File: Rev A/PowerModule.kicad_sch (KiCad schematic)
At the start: 20 parts, among them K1 Relay_SPDT, Q1 IRLZ44N, U1 LM741

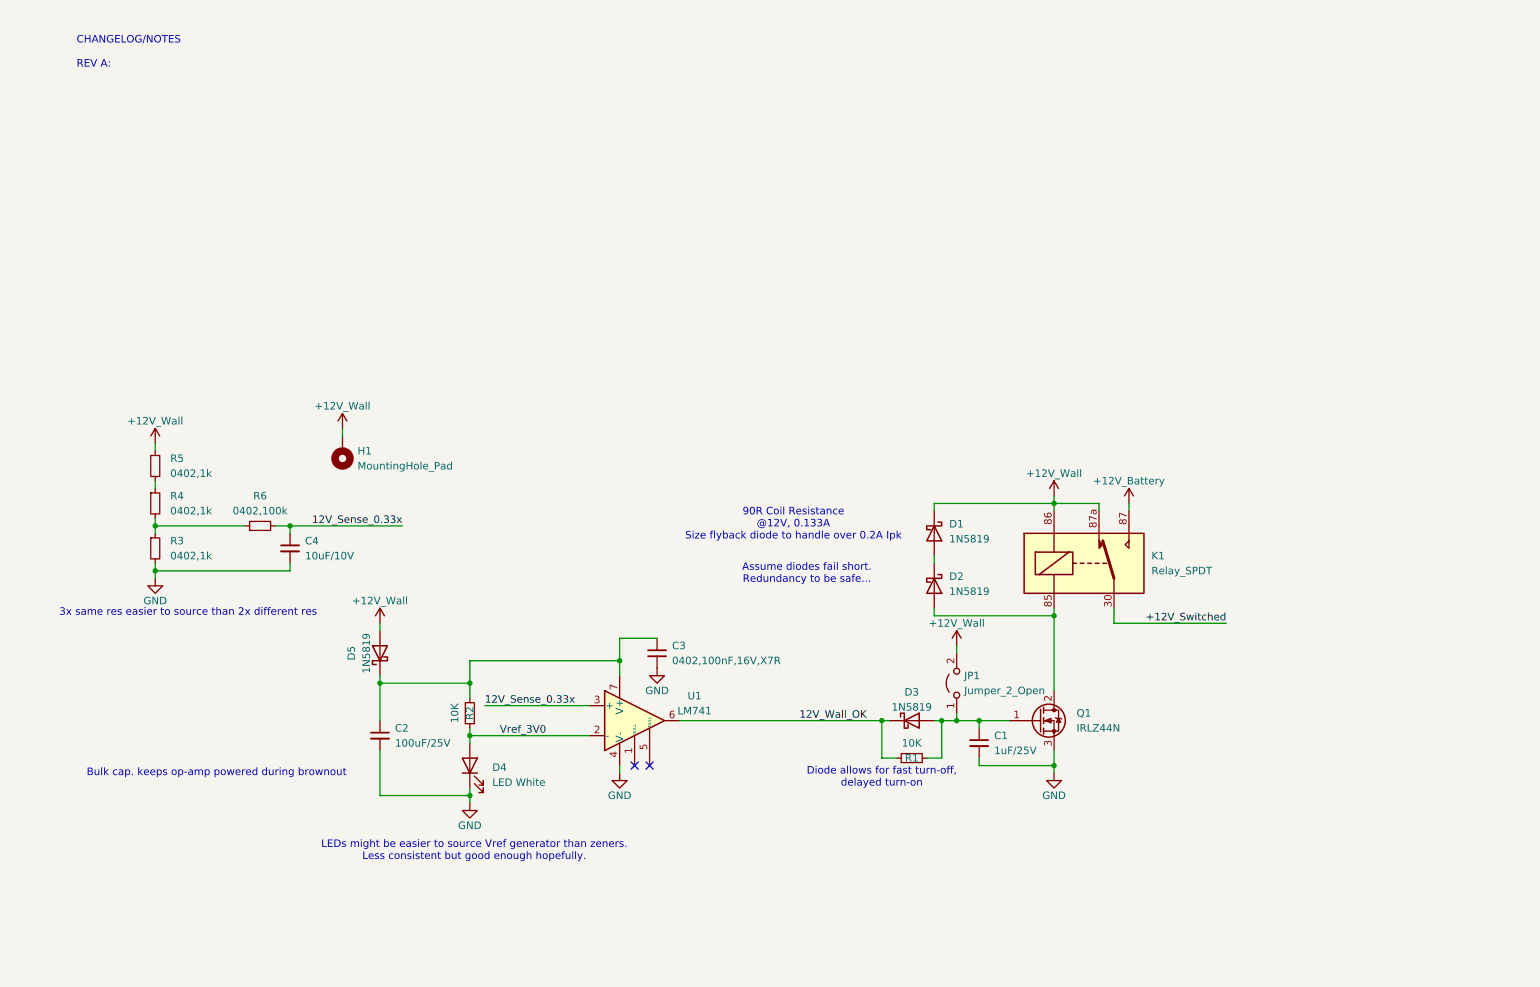
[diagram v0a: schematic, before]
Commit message: added simulation stuff
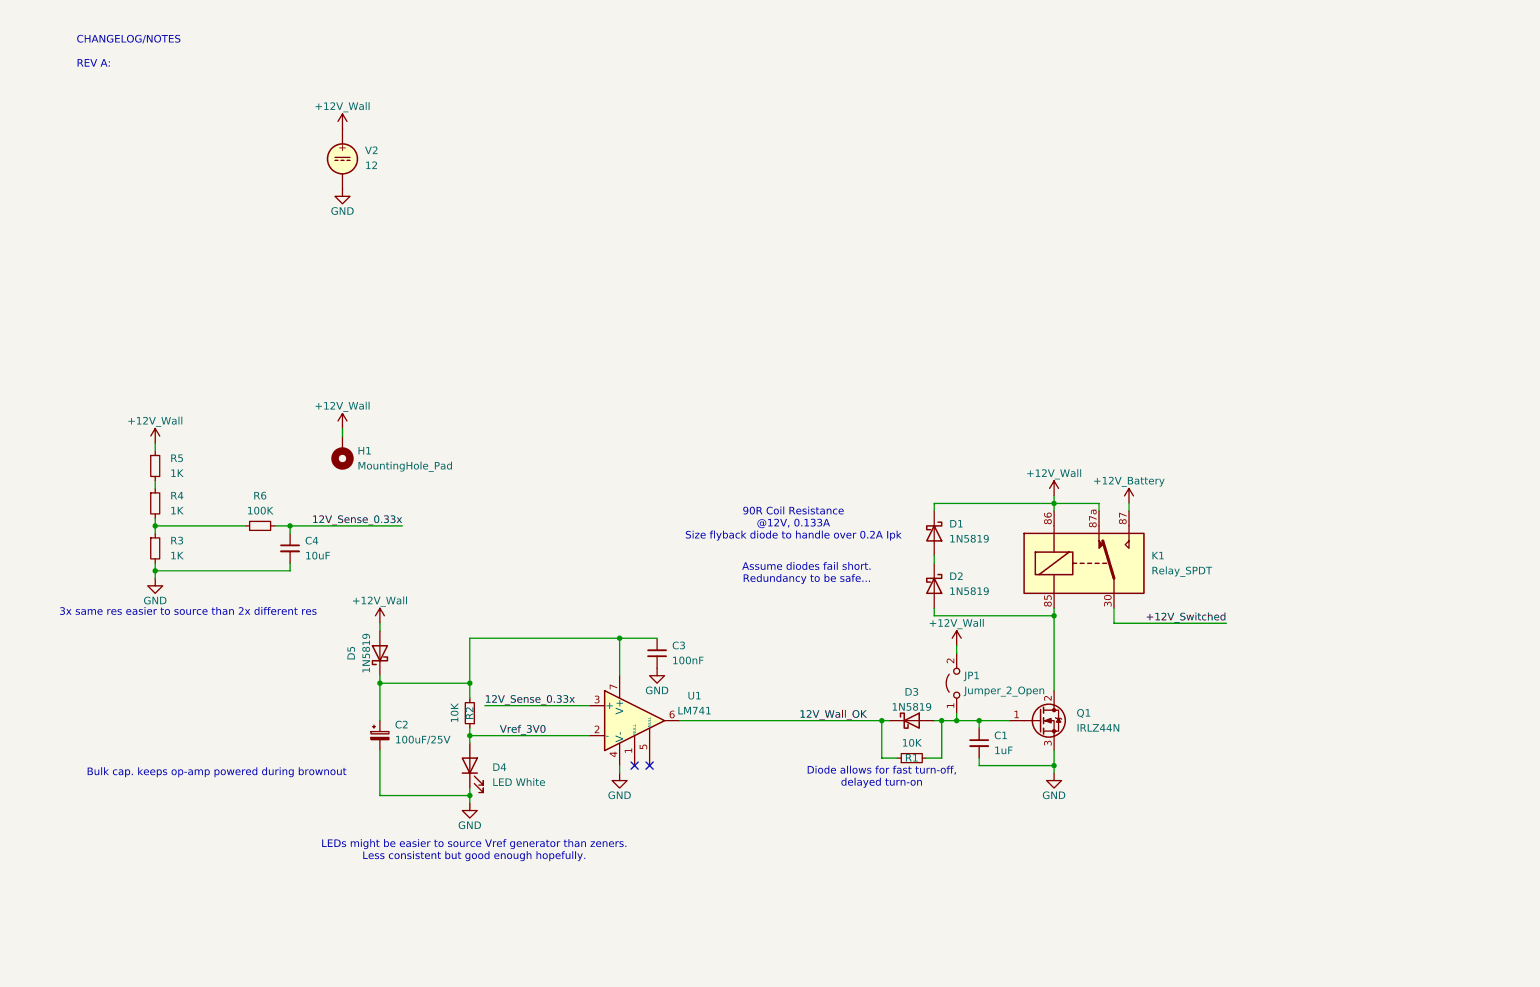
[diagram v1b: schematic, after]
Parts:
- removed C2: 100uF/25V, symbol Device:C_Small
- added C2: 100uF/25V, symbol Device:C_Polarized_Small
- added V2: 12, symbol Simulation_SPICE:VDC
- C1: value 1uF/25V -> 1uF
- C3: value 0402,100nF,16V,X7R -> 100nF
- C4: value 10uF/10V -> 10uF
- R3, R4, R5: value 0402,1k -> 1K
- R6: value 0402,100k -> 100K
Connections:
- net +12V_Wall: now also V2.1
- net GND: now also C2.2, V2.2
- net at C3.1, D5.1 (K), R2.2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: now also C2.1

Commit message: Added all schematic parts, started layout
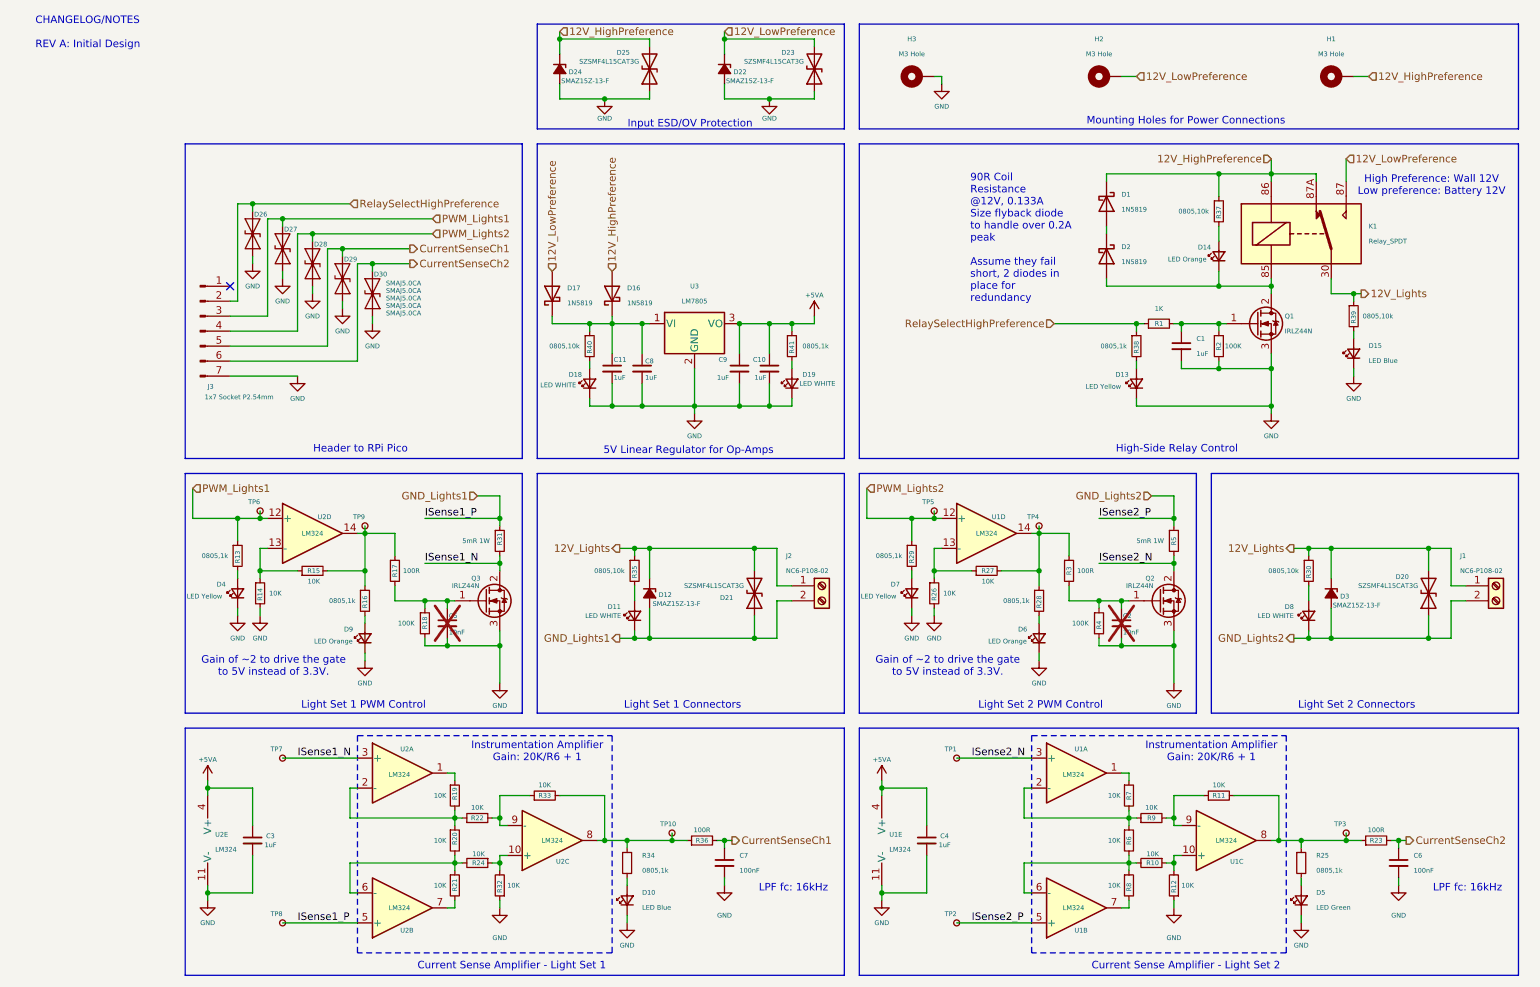
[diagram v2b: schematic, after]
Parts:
- removed C2: 100uF/25V, symbol Device:C_Polarized_Small
- removed C3: 100nF, C_0402_1005Metric, symbol jlcpcb-basic-capacitor:0402,100nF,16V,X7R
- removed D3, D5: 1N5819, Diode_THT:D_DO-41_SOD81_P10.16mm_Horizontal, symbol Diode:1N5819
- removed D4: LED White, symbol Device:LED
- removed JP1: Jumper_2_Open, symbol Jumper:Jumper_2_Open
- removed R1, R2: 10K, symbol Device:R_Small
- removed R4, R5: 1K, R_0402_1005Metric, symbol jlcpcb-basic-resistor:0402,1k
- removed R6: 100K, R_0402_1005Metric, symbol jlcpcb-basic-resistor:0402,100k
- removed U1: LM741, symbol Amplifier_Operational:LM741
- removed V2: 12, symbol Simulation_SPICE:VDC
- added C10, C11, C3, C8, C9: 1uF, Capacitor_SMD:C_0805_2012Metric, symbol Device:C_Small
- added C2, C5: 10nF, Capacitor_SMD:C_0805_2012Metric, symbol Device:C_Small
- added C6, C7: 100nF, Capacitor_SMD:C_0805_2012Metric, symbol Device:C_Small
- added D10, D15: LED Blue, LED_SMD:LED_0805_2012Metric, symbol Device:LED_Small
- added D11, D18, D19, D8: LED WHITE, LED_SMD:LED_0805_2012Metric, symbol Device:LED_Small
- added D12, D22, D24, D3: SMAZ15Z-13-F, Diode_SMD:D_SMA, symbol Device:D_Zener_Small_Filled
- added D13, D4, D7: LED Yellow, LED_SMD:LED_0805_2012Metric, symbol Device:LED_Small
- added D14, D6, D9: LED Orange, LED_SMD:LED_0805_2012Metric, symbol Device:LED_Small
- added D16, D17: 1N5819, Diode_THT:D_DO-41_SOD81_P10.16mm_Horizontal, symbol Diode:1N5819
- added D20, D21, D23, D25: SZSMF4L15CAT3G, Diode_SMD:D_SOD-123F, symbol Device:D_TVS
- added D26, D27, D28, D29, D30: SMAJ5.0CA, Diode_SMD:D_SMA, symbol Diode:SMAJ5.0CA
- added D5: LED Green, LED_SMD:LED_0805_2012Metric, symbol Device:LED_Small
- added H2, H3: M3 Hole, MountingHole:MountingHole_3.2mm_M3_Pad_TopBottom, symbol Mechanical:MountingHole_Pad
- added J1, J2: NC6-P108-02, TerminalBlock_MetzConnect:TerminalBlock_MetzConnect_Type703_RT10N02HGLU_1x02_P9.52mm_Horizontal, symbol Connector:Screw_Terminal_01x02
- added J3: 1x7 Socket P2.54mm, Connector_PinSocket_2.54mm:PinSocket_1x07_P2.54mm_Vertical, symbol Connector:Conn_01x07_Pin
- added Q2, Q3: IRLZ44N, Package_TO_SOT_THT:TO-220-3_Horizontal_TabDown, symbol Transistor_FET:IRLZ44N
- added R1: 1K, Resistor_SMD:R_0805_2012Metric, symbol jlcpcb-basic-resistor:0402,1k
- added R10, R11, R12, R14, R15, R19, R20, R21, R22, R24, R26, R27, R32, R33, R6, R7, R8, R9: 10K, Resistor_SMD:R_0805_2012Metric, symbol jlcpcb-basic-resistor:0402,10k
- added R13, R16, R25, R28, R29, R34, R38, R41: 0805,1k, Resistor_SMD:R_0805_2012Metric, symbol jlcpcb-basic-resistor:0805,1k
- added R17: 100R, Resistor_SMD:R_0805_2012Metric, symbol jlcpcb-basic-resistor:0402,1k
- added R18, R2, R4: 100K, Resistor_SMD:R_0805_2012Metric, symbol jlcpcb-basic-resistor:0402,100k
- added R23, R36: 100R, Resistor_SMD:R_0805_2012Metric, symbol jlcpcb-basic-resistor:0402,10k
- added R30, R35, R37, R39, R40: 0805,10k, Resistor_SMD:R_0805_2012Metric, symbol jlcpcb-basic-resistor:0805,10k
- added R31, R5: 5mR 1W, Resistor_SMD:R_2512_6332Metric, symbol Device:R_Small
- added TP1, TP10, TP2, TP3, TP4, TP5, TP6, TP7, TP8, TP9: TestPoint_Small, TestPoint:TestPoint_Pad_D2.0mm, symbol Connector:TestPoint_Small
- added U1, U2: LM324, Package_DIP:DIP-14_W7.62mm_Socket, symbol Amplifier_Operational:LM324
- added U3: LM7805, Package_TO_SOT_THT:TO-220-3_Horizontal_TabDown, symbol Regulator_Linear:LM7805_TO220
- C1: footprint (none) -> Capacitor_SMD:C_0805_2012Metric
- C4: value 10uF -> 1uF; footprint (none) -> Capacitor_SMD:C_0805_2012Metric
- H1: value MountingHole_Pad -> M3 Hole; footprint (none) -> MountingHole:MountingHole_3.2mm_M3_Pad_TopBottom; now left out of the parts list
- Q1: footprint Package_TO_SOT_THT:TO-220-3_Vertical -> Package_TO_SOT_THT:TO-220-3_Horizontal_TabDown
- R3: value 1K -> 100R; footprint R_0402_1005Metric -> Resistor_SMD:R_0805_2012Metric
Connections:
- net GND: now also C10.2, C11.2, C2.2, C3.2, C5.2, C6.2, C7.2, C8.2, C9.2, D10.1 (K), D13.1 (K), D15.1 (K), D18.1 (K), D19.1 (K), D22.2 (A), D23.1 (A1), D24.2 (A), D25.1 (A1), D26.1 (A1), D27.1 (A1), D28.1 (A1), D29.1 (A1), D30.1 (A1), D4.1 (K), D5.1 (K), D6.1 (K), D7.1 (K), D9.1 (K), H3.1, J3.7 (Pin_7), Q2.3 (S), Q3.3 (S), R12.1, R14.2, R18.2, R2.2, R26.2, R32.1, R4.2, U1.11 (V-), U2.11 (V-), U3.2 (GND); no longer R3.2
- net at C1.1, Q1.1 (G): now also R1.2, R2.1
- net at D2.2 (A), K1.85, Q1.2 (D): now also D14.1 (K)
- net at R3.1: now also R27.2, R28.1, TP4.1, U1.14
- net +12V_Battery renamed 12V_LowPreference
- net 12V_LowPreference: now also D17.2 (A), D22.1 (K), D23.2 (A2), H2.1
- net +12V_Switched renamed 12V_Lights
- net 12V_Lights: now also D12.1 (K), D20.2 (A2), D21.2 (A2), D3.1 (K), J1.1 (Pin_1), J2.1 (Pin_1), R30.1, R35.1, R39.1
- net +12V_Wall renamed 12V_HighPreference
- net 12V_HighPreference: now also K1.87A, D16.2 (A), D24.1 (K), D25.2 (A2), R37.1; no longer K1.87a
- net 12V_Sense_0.33x renamed +5VA
- net +5VA: now also C10.1, C3.1, C9.1, R41.1, U1.4 (V+), U2.4 (V+), U3.3 (VO)
- new net: D7.2 (A), R29.2
- new net: R19.1, U2.1
- new net: R19.2, R20.1, R22.1, U2.2 (-)
- new net: R33.2, R34.1, R36.1, TP10.1, U2.8
- new net: R15.2, R16.1, R17.1, TP9.1, U2.14
- new net: C5.1, Q3.1 (G), R17.2, R18.1
- new net: D15.2 (A), R39.2
- new net: R22.2, R33.1, U2.9 (-)
- new net: D13.2 (A), R38.2
- new net: R7.1, U1.1
- new net: R6.1, R7.2, R9.1, U1.2 (-)
- new net: C2.1, Q2.1 (G), R3.2, R4.1
- new net: R11.2, R23.1, R25.1, TP3.1, U1.8
- new net: R10.1, R12.2, U1.10 (+)
- new net: R10.2, R6.2, R8.1, U1.6 (-)
- new net: R8.2, U1.7
- new net: C11.1, C8.1, D16.1 (K), D17.1 (K), R40.1, U3.1 (VI)
- new net: R24.1, R32.2, U2.10 (+)
- new net: R20.2, R21.1, R24.2, U2.6 (-)
- new net: D5.2 (A), R25.2
- new net: D14.2 (A), R37.2
- new net: D4.2 (A), R13.2
- new net: R21.2, U2.7
- new net: R11.1, R9.2, U1.9 (-)
- new net: R26.1, R27.1, U1.13 (-)
- new net: D9.2 (A), R16.2
- new net: R14.1, R15.1, U2.13 (-)
- new net: D8.2 (A), R30.2
- new net: D10.2 (A), R34.2
- new net: D11.2 (A), R35.2
- new net: D19.2 (A), R41.2
- new net: D6.2 (A), R28.2
- new net: D18.2 (A), R40.2
- new net CurrentSenseCh1: C7.1, D29.2 (A2), J3.5 (Pin_5), R36.2
- new net CurrentSenseCh2: C6.1, D30.2 (A2), J3.6 (Pin_6), R23.2
- new net GND_Lights1: D11.1 (K), D12.2 (A), D21.1 (A1), J2.2 (Pin_2), R31.1, TP8.1, U2.5 (+)
- new net GND_Lights2: D20.1 (A1), D3.2 (A), D8.1 (K), J1.2 (Pin_2), R5.1, TP2.1, U1.5 (+)
- new net ISense1_N: Q3.2 (D), R31.2, TP7.1, U2.3 (+)
- new net ISense2_N: Q2.2 (D), R5.2, TP1.1, U1.3 (+)
- new net PWM_Lights1: D27.2 (A2), J3.3 (Pin_3), R13.1, TP6.1, U2.12 (+)
- new net PWM_Lights2: D28.2 (A2), J3.4 (Pin_4), R29.1, TP5.1, U1.12 (+)
- new net RelaySelectHighPreference: D26.2 (A2), J3.2 (Pin_2), R1.1, R38.1
- no-connect marks 2 -> 1
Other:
- note added: "5V Linear Regulator for Op-Amps"
- note added: "CHANGELOG/NOTES REV A: Initial Design"
- note added: "Current Sense Amplifier - Light Set 1"
- note added: "Current Sense Amplifier - Light Set 2"
- note added: "Gain of ~2 to drive the gate to 5V instead of 3.3V."
- note added: "Header to RPi Pico"
- note added: "High Preference: Wall 12V Low preference: Battery 12V"
- note added: "High-Side Relay Control"
- note added: "Input ESD/OV Protection"
- note added: "Instrumentation Amplifier Gain: 20K/R6 + 1"
- note added: "LPF fc: 16kHz"
- note added: "Light Set 1 Connectors"
- note added: "Light Set 1 PWM Control"
- note added: "Light Set 2 Connectors"
- note added: "Light Set 2 PWM Control"
- note added: "Mounting Holes for Power Connections"
- note removed: "3x same res easier to source than 2x different res"
- note removed: "90R Coil Resistance @12V, 0.133A Size flyback diode to handle over 0.2A Ipk"
- note removed: "Assume diodes fail short. Redundancy to be safe..."
- note removed: "Bulk cap. keeps op-amp powered during brownout"
- note removed: "CHANGELOG/NOTES REV A:"
- note removed: "Diode allows for fast turn-off, delayed turn-on"
- note removed: "LEDs might be easier to source Vref generator than zeners. Less consistent but good enough hopefully."
- moved on the sheet: C1, D1, D2, K1, Q1

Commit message: laid out pcb
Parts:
- added H4: M3 Hole, MountingHole:MountingHole_3.2mm_M3_Pad_TopBottom, symbol Mechanical:MountingHole_Pad
- added R42: 0805,0, R_0805_2012Metric, symbol jlcpcb-basic-resistor:0805,0
- C6, C7: value 100nF -> 10nF
- D1, D16, D17, D2: value 1N5819 -> 1N5819W; footprint Diode_THT:D_DO-41_SOD81_P10.16mm_Horizontal -> Diode_SMD:D_SOD-123F
- D10: value LED Blue -> LED Green
- D26, D27, D28, D29, D30: value SMAJ5.0CA -> PESD3V3L1BA,115; footprint Diode_SMD:D_SMA -> Diode_SMD:D_SOD-323F
- R23, R36: value 100R -> 1K
- U3: now not fitted
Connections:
- net CurrentSenseCh1: now also C6.1, R23.2, TP3.1; no longer C7.1, R36.2
- net CurrentSenseCh2: now also C7.1, R36.2, TP10.1; no longer C6.1, R23.2
- net GND: now also H4.1
- net GND_Lights1: now also D20.1 (A1), D3.2 (A), D8.1 (K), J1.2 (Pin_2), R5.1, TP2.1, U1.5 (+); no longer D11.1 (K), D12.2 (A), D21.1 (A1), J2.2 (Pin_2), R31.1, TP8.1, U2.5 (+)
- net GND_Lights2: now also D11.1 (K), D12.2 (A), D21.1 (A1), J2.2 (Pin_2), R31.1, TP8.1, U2.5 (+); no longer D20.1 (A1), D3.2 (A), D8.1 (K), J1.2 (Pin_2), R5.1, TP2.1, U1.5 (+)
- net ISense1_N: now also Q2.2 (D), R5.2, TP1.1, U1.3 (+); no longer Q3.2 (D), R31.2, TP7.1, U2.3 (+)
- net ISense2_N: now also Q3.2 (D), R31.2, TP7.1, U2.3 (+); no longer Q2.2 (D), R5.2, TP1.1, U1.3 (+)
- net PWM_Lights1: now also R29.1, TP5.1, U1.12 (+); no longer R13.1, TP6.1, U2.12 (+)
- net PWM_Lights2: now also R13.1, TP6.1, U2.12 (+); no longer R29.1, TP5.1, U1.12 (+)
- net ISen2_unfilt: now reaches R33.2, R34.1, R36.1, U2.8
- net ISen2_unfilt: no longer TP10.1
- net at R15.2, R16.1, R17.1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: no longer TP9.1
- net at C5.1, Q3.1 (G), R17.2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: now also TP9.1
- net at C2.1, Q2.1 (G), R3.2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: now also TP4.1
- net ISen1_unfilt: now reaches R11.2, R23.1, R25.1, U1.8
- net ISen1_unfilt: no longer TP3.1
- net VIN_OPA_PWR: now reaches C11.1, C8.1, D16.1 (K), D17.1 (K), R40.1, U3.1 (VI)
- net VIN_OPA_PWR: now also R42.1
- net at R27.2, R28.1, R3.1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: no longer TP4.1
- net +5VA renamed OpAmpPWR
- net OpAmpPWR: now also R42.2
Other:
- moved on the sheet: C11, D16, R18, R23, R4, TP10, TP3
